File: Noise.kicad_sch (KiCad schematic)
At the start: 13 parts, among them P5 10k, Q1 BC183, Q2 BFY33

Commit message: Fix PCB errors
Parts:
- added C26: 1uF, Capacitor_THT:CP_Radial_D6.3mm_P2.50mm, symbol Device:C_Polarized
- added C_Sin1 (x2): Conn_01x01, Connector_PinHeader_2.54mm:PinHeader_1x01_P2.54mm_Vertical, symbol Connector_Generic:Conn_01x01
- added R16: 15k, Resistor_THT:R_Axial_DIN0207_L6.3mm_D2.5mm_P15.24mm_Horizontal, symbol Device:R
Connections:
- net NOISE_LEVEL: now also R16.2; no longer P5.2
- net at C1.2, P5.1: now also C_Sin1.1 (Pin_1)
- new net: C26.1, R16.1
- new net: C26.2, C_Sin1.1 (Pin_1), P5.2
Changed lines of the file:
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@@
 (kicad_sch (version 20230121) (generator eeschema)
   (paper "A4")
+  (junction (at 137.795 54.61) (diameter 0) (color 0 0 0 0)
+  )
   (junction (at 111.76 49.53) (diameter 0) (color 0 0 0 0)
   )
+  (junction (at 132.715 49.53) (diameter 0) (color 0 0 0 0)
+  )
   (junction (at 92.71 55.88) (diameter 0) (color 0 0 0 0)
   )
@@
   )
   (no_connect (at 85.09 60.96))
+  (wire (pts (xy 159.385 54.61) (xy 161.29 54.61))
+    (stroke (width 0) (type default))
+  )
   (wire (pts (xy 111.76 60.96) (xy 120.65 60.96))
     (stroke (width 0) (type default))
@@
     (stroke (width 0) (type default))
   )
-  (wire (pts (xy 136.525 54.61) (xy 140.97 54.61))
+  (wire (pts (xy 136.525 54.61) (xy 137.795 54.61))
     (stroke (width 0) (type default))
   )
@@
     (stroke (width 0) (type default))
   )
+  (wire (pts (xy 137.795 54.61) (xy 140.97 54.61))
+    (stroke (width 0) (type default))
+  )
   (wire (pts (xy 73.66 54.61) (xy 73.66 52.07))
     (stroke (width 0) (type default))
@@
     (stroke (width 0) (type default))
   )
+  (wire (pts (xy 148.59 54.61) (xy 151.765 54.61))
+    (stroke (width 0) (type default))
+  )
   (wire (pts (xy 111.76 50.8) (xy 111.76 49.53))
     (stroke (width 0) (type default))
   )
-  (global_label "NOISE_LEVEL" (shape input) (at 140.97 54.61 0)
+  (global_label "NOISE_LEVEL" (shape input) (at 161.29 54.61 0)
     (effects (font (size 1.27 1.27)) (justify left))
-    (property "Intersheetrefs" "${INTERSHEET_REFS}" (at 140.97 54.61 0)
+    (property "Intersheetrefs" "${INTERSHEET_REFS}" (at 161.29 54.61 0)
       (effects (font (size 1.27 1.27)) hide)
     )
@@
     )
   )
+  (symbol (lib_id "Device:R") (at 155.575 54.61 90) (mirror x) (unit 1)
+    (in_bom yes) (on_board yes) (dnp no)
+    (property "Reference" "R16" (at 154.4066 56.388 0)
+      (effects (font (size 1.27 1.27)) (justify left))
+    )
+    (property "Value" "15k" (at 156.718 56.388 0)
+      (effects (font (size 1.27 1.27)) (justify left))
+    )
+    (property "Footprint" "Resistor_THT:R_Axial_DIN0207_L6.3mm_D2.5mm_P15.24mm_Horizontal" (at 155.575 52.832 90)
+      (effects (font (size 1.27 1.27)) hide)
+    )
+    (property "Datasheet" "~" (at 155.575 54.61 0)
+      (effects (font (size 1.27 1.27)) hide)
+    )
+    (pin "1")
+    (pin "2")
+    (instances
+      (project "janel-panel-minimoog"
+        (path "/3cc2a3de-1ac5-4269-8b63-e6b812b486d5/00000000-0000-0000-0000-00005e0fcafc"
+          (reference "R16") (unit 1)
+        )
+      )
+    )
+  )
+  (symbol (lib_id "Device:C_Polarized") (at 144.78 54.61 270) (unit 1)
+    (in_bom yes) (on_board yes) (dnp no) (fields_autoplaced)
+    (property "Reference" "C26" (at 145.669 48.26 90)
+      (effects (font (size 1.27 1.27)))
+    )
+    (property "Value" "1uF" (at 145.669 50.8 90)
+      (effects (font (size 1.27 1.27)))
+    )
+    (property "Footprint" "Capacitor_THT:CP_Radial_D6.3mm_P2.50mm" (at 140.97 55.5752 0)
+      (effects (font (size 1.27 1.27)) hide)
+    )
+    (property "Datasheet" "~" (at 144.78 54.61 0)
+      (effects (font (size 1.27 1.27)) hide)
+    )
+    (pin "1")
+    (pin "2")
+    (instances
+      (project "janel-panel-minimoog"
+        (path "/3cc2a3de-1ac5-4269-8b63-e6b812b486d5/00000000-0000-0000-0000-00005e0fcafc"
+          (reference "C26") (unit 1)
+        )
+      )
+    )
+  )
+  (symbol (lib_id "Connector_Generic:Conn_01x01") (at 137.795 59.69 270) (unit 1)
+    (in_bom yes) (on_board yes) (dnp no) (fields_autoplaced)
+    (property "Reference" "C_Sin1" (at 140.97 59.055 90)
+      (effects (font (size 1.27 1.27)) (justify left))
+    )
+    (property "Value" "Conn_01x01" (at 140.97 61.595 90)
+      (effects (font (size 1.27 1.27)) (justify left))
+    )
+    (property "Footprint" "Connector_PinHeader_2.54mm:PinHeader_1x01_P2.54mm_Vertical" (at 137.795 59.69 0)
+      (effects (font (size 1.27 1.27)) hide)
+    )
+    (property "Datasheet" "~" (at 137.795 59.69 0)
+      (effects (font (size 1.27 1.27)) hide)
+    )
+    (pin "1")
+    (instances
+      (project "janel-panel-minimoog"
+        (path "/3cc2a3de-1ac5-4269-8b63-e6b812b486d5/00000000-0000-0000-0000-00005e37b0c8"
+          (reference "C_Sin1") (unit 1)
+        )
+        (path "/3cc2a3de-1ac5-4269-8b63-e6b812b486d5/00000000-0000-0000-0000-00005e12e25c"
+          (reference "C_Sin2") (unit 1)
+        )
+        (path "/3cc2a3de-1ac5-4269-8b63-e6b812b486d5/00000000-0000-0000-0000-00005e0fcafc"
+          (reference "P5-3") (unit 1)
+        )
+      )
+    )
+  )
   (symbol (lib_id "Device:R_Potentiometer") (at 132.715 54.61 0) (unit 1)
-    (in_bom yes) (on_board yes) (dnp no) (fields_autoplaced)
+    (in_bom yes) (on_board no) (dnp no) (fields_autoplaced)
     (property "Reference" "P5" (at 130.81 53.975 0)
       (effects (font (size 1.27 1.27)) (justify right))
@@
         )
       )
+    )
+  )
+  (symbol (lib_id "Connector_Generic:Conn_01x01") (at 132.715 44.45 90) (unit 1)
+    (in_bom yes) (on_board yes) (dnp no) (fields_autoplaced)
+    (property "Reference" "C_Sin1" (at 135.89 43.815 90)
+      (effects (font (size 1.27 1.27)) (justify right))
+    )
+    (property "Value" "Conn_01x01" (at 135.89 46.355 90)
+      (effects (font (size 1.27 1.27)) (justify right))
+    )
+    (property "Footprint" "Connector_PinHeader_2.54mm:PinHeader_1x01_P2.54mm_Vertical" (at 132.715 44.45 0)
+      (effects (font (size 1.27 1.27)) hide)
+    )
+    (property "Datasheet" "~" (at 132.715 44.45 0)
+      (effects (font (size 1.27 1.27)) hide)
+    )
+    (pin "1")
+    (instances
+      (project "janel-panel-minimoog"
+        (path "/3cc2a3de-1ac5-4269-8b63-e6b812b486d5/00000000-0000-0000-0000-00005e37b0c8"
+          (reference "C_Sin1") (unit 1)
+        )
+        (path "/3cc2a3de-1ac5-4269-8b63-e6b812b486d5/00000000-0000-0000-0000-00005e12e25c"
+          (reference "C_Sin2") (unit 1)
+        )
+        (path "/3cc2a3de-1ac5-4269-8b63-e6b812b486d5/00000000-0000-0000-0000-00005e0fcafc"
+          (reference "P5-1") (unit 1)
+        )
+      )

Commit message: Kicad update
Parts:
- renumbered C_Sin1 to P5-1, C_Sin1 to P5-3

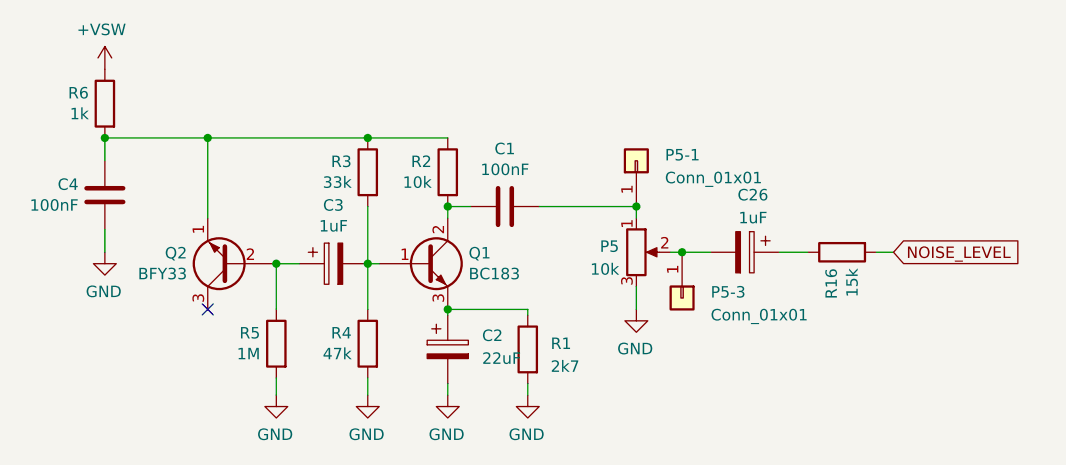
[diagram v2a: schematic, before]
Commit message: Replace symbols with new library
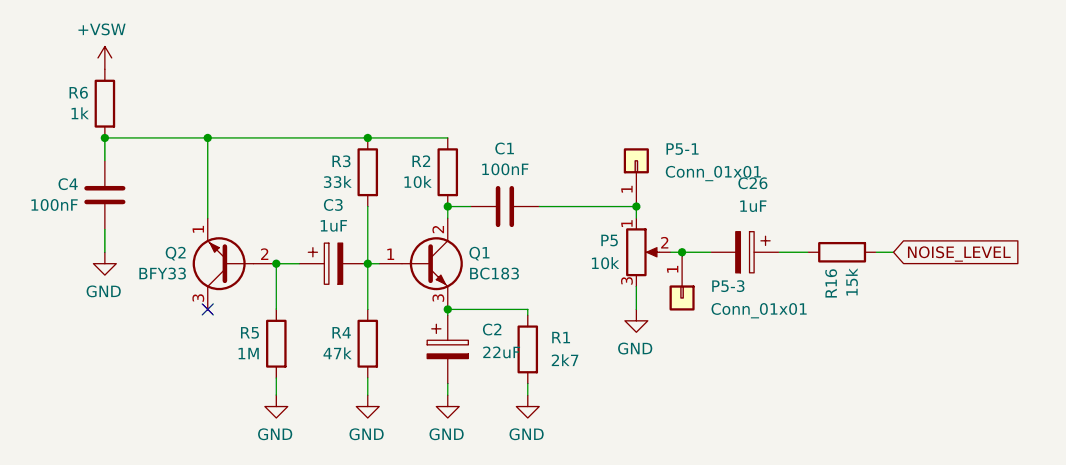
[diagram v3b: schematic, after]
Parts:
- C1, C4: footprint Capacitor_THT:C_Disc_D5.0mm_W2.5mm_P5.00mm -> (none)
- C2, C26, C3: footprint Capacitor_THT:CP_Radial_D6.3mm_P2.50mm -> (none)
- P5: footprint Connector_PinSocket_2.54mm:PinSocket_1x03_P2.54mm_Vertical -> (none)
- P5-1, P5-3: footprint Connector_PinHeader_2.54mm:PinHeader_1x01_P2.54mm_Vertical -> (none)
- Q1: symbol Device:Q_NPN_BCE -> Transistor_BJT:Q_NPN_BCE
- Q2: footprint Package_TO_SOT_THT:TO-92L_Inline_Wide -> Package_TO_SOT_THT:TO-92_Inline
- R1, R16, R2, R3, R4, R5, R6: footprint Resistor_THT:R_Axial_DIN0207_L6.3mm_D2.5mm_P15.24mm_Horizontal -> (none)

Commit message: Label connectors, update footprints
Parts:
- C1, C4: footprint (none) -> Capacitor_THT:C_Disc_D5.0mm_W2.5mm_P5.00mm
- C2, C26, C3: footprint (none) -> Capacitor_THT:CP_Radial_D6.3mm_P2.50mm
- P5-1, P5-3: footprint (none) -> Connector_PinHeader_2.54mm:PinHeader_1x01_P2.54mm_Vertical
- R1, R16, R2, R3, R4, R5, R6: footprint (none) -> Resistor_THT:R_Axial_DIN0207_L6.3mm_D2.5mm_P15.24mm_Horizontal
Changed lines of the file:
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@@
 			)
 		)
-		(property "Footprint" ""
+		(property "Footprint" "Resistor_THT:R_Axial_DIN0207_L6.3mm_D2.5mm_P15.24mm_Horizontal"
 			(at 104.648 45.72 90)
 			(effects
@@
 			)
 		)
-		(property "Footprint" ""
+		(property "Footprint" "Resistor_THT:R_Axial_DIN0207_L6.3mm_D2.5mm_P15.24mm_Horizontal"
 			(at 113.538 45.72 90)
 			(effects
@@
 			)
 		)
-		(property "Footprint" ""
+		(property "Footprint" "Resistor_THT:R_Axial_DIN0207_L6.3mm_D2.5mm_P15.24mm_Horizontal"
 			(at 122.428 65.405 90)
 			(effects
@@
 			)
 		)
-		(property "Footprint" ""
+		(property "Footprint" "Resistor_THT:R_Axial_DIN0207_L6.3mm_D2.5mm_P15.24mm_Horizontal"
 			(at 75.438 38.1 90)
 			(effects
@@
 			)
 		)
-		(property "Footprint" ""
+		(property "Footprint" "Resistor_THT:R_Axial_DIN0207_L6.3mm_D2.5mm_P15.24mm_Horizontal"
 			(at 104.648 64.77 90)
 			(effects
@@
 			)
 		)
-		(property "Footprint" ""
+		(property "Footprint" "Resistor_THT:R_Axial_DIN0207_L6.3mm_D2.5mm_P15.24mm_Horizontal"
 			(at 94.488 64.77 90)
 			(effects
@@
 			)
 		)
-		(property "Footprint" ""
+		(property "Footprint" "Capacitor_THT:C_Disc_D5.0mm_W2.5mm_P5.00mm"
 			(at 121.92 50.4952 0)
 			(effects
@@
 			)
 		)
-		(property "Footprint" ""
+		(property "Footprint" "Capacitor_THT:CP_Radial_D6.3mm_P2.50mm"
 			(at 102.87 56.8452 0)
 			(effects
@@
 			)
 		)
-		(property "Footprint" ""
+		(property "Footprint" "Capacitor_THT:C_Disc_D5.0mm_W2.5mm_P5.00mm"
 			(at 72.6948 52.07 0)
 			(effects
@@
 			)
 		)
-		(property "Footprint" ""
+		(property "Footprint" "Resistor_THT:R_Axial_DIN0207_L6.3mm_D2.5mm_P15.24mm_Horizontal"
 			(at 155.575 52.832 90)
 			(effects
@@
 			)
 		)
-		(property "Footprint" ""
+		(property "Footprint" "Capacitor_THT:CP_Radial_D6.3mm_P2.50mm"
 			(at 140.97 55.5752 0)
 			(effects
@@
 			)
 		)
-		(property "Footprint" ""
+		(property "Footprint" "Connector_PinHeader_2.54mm:PinHeader_1x01_P2.54mm_Vertical"
 			(at 137.795 59.69 0)
 			(effects
@@
 			)
 		)
-		(property "Footprint" ""
+		(property "Footprint" "Connector_PinHeader_2.54mm:PinHeader_1x01_P2.54mm_Vertical"
 			(at 132.715 44.45 0)
 			(effects
@@
 			)
 		)
-		(property "Footprint" ""
+		(property "Footprint" "Capacitor_THT:CP_Radial_D6.3mm_P2.50mm"
 			(at 112.7252 69.215 0)
 			(effects
